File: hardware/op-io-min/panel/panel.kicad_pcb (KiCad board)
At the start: 2 copper layers, 20.3 x 128.5 mm, 3 parts

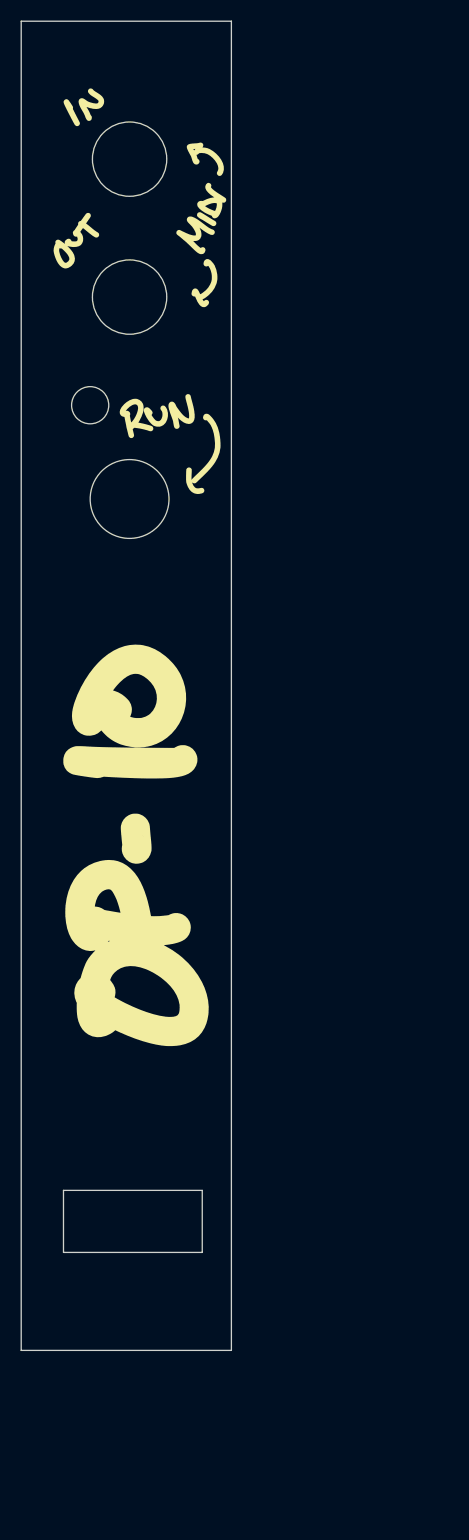
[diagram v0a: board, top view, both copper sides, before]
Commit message: added output impedance resistor
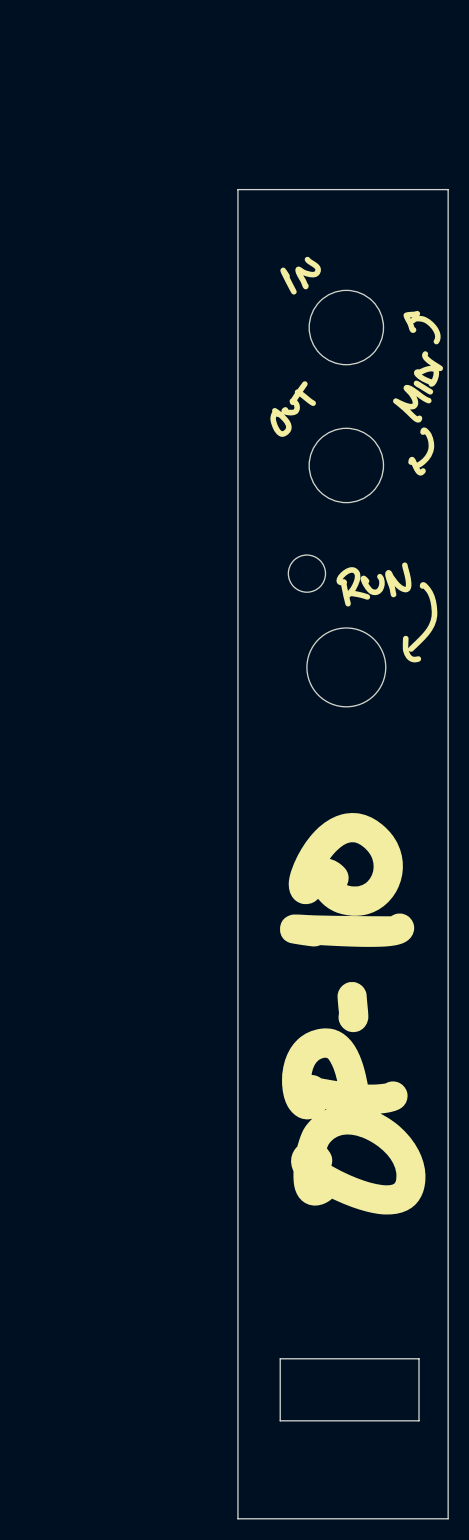
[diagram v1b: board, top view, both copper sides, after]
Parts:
- moved   26.5 mm to (28.5, 19.3)
- moved   26.5 mm to (28.5, 141.8)
- moved ? 26.5 mm to (21.7, 15.2)
